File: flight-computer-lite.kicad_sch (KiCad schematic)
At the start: 18 parts, among them J1 USB_C_Receptacle_USB2.0_16P, J2 Micro_SD_Card_Det2, J3 Conn_01x02_Pin, Q1 BSS138, U1 RP2040, U2 W25Q32JVZP

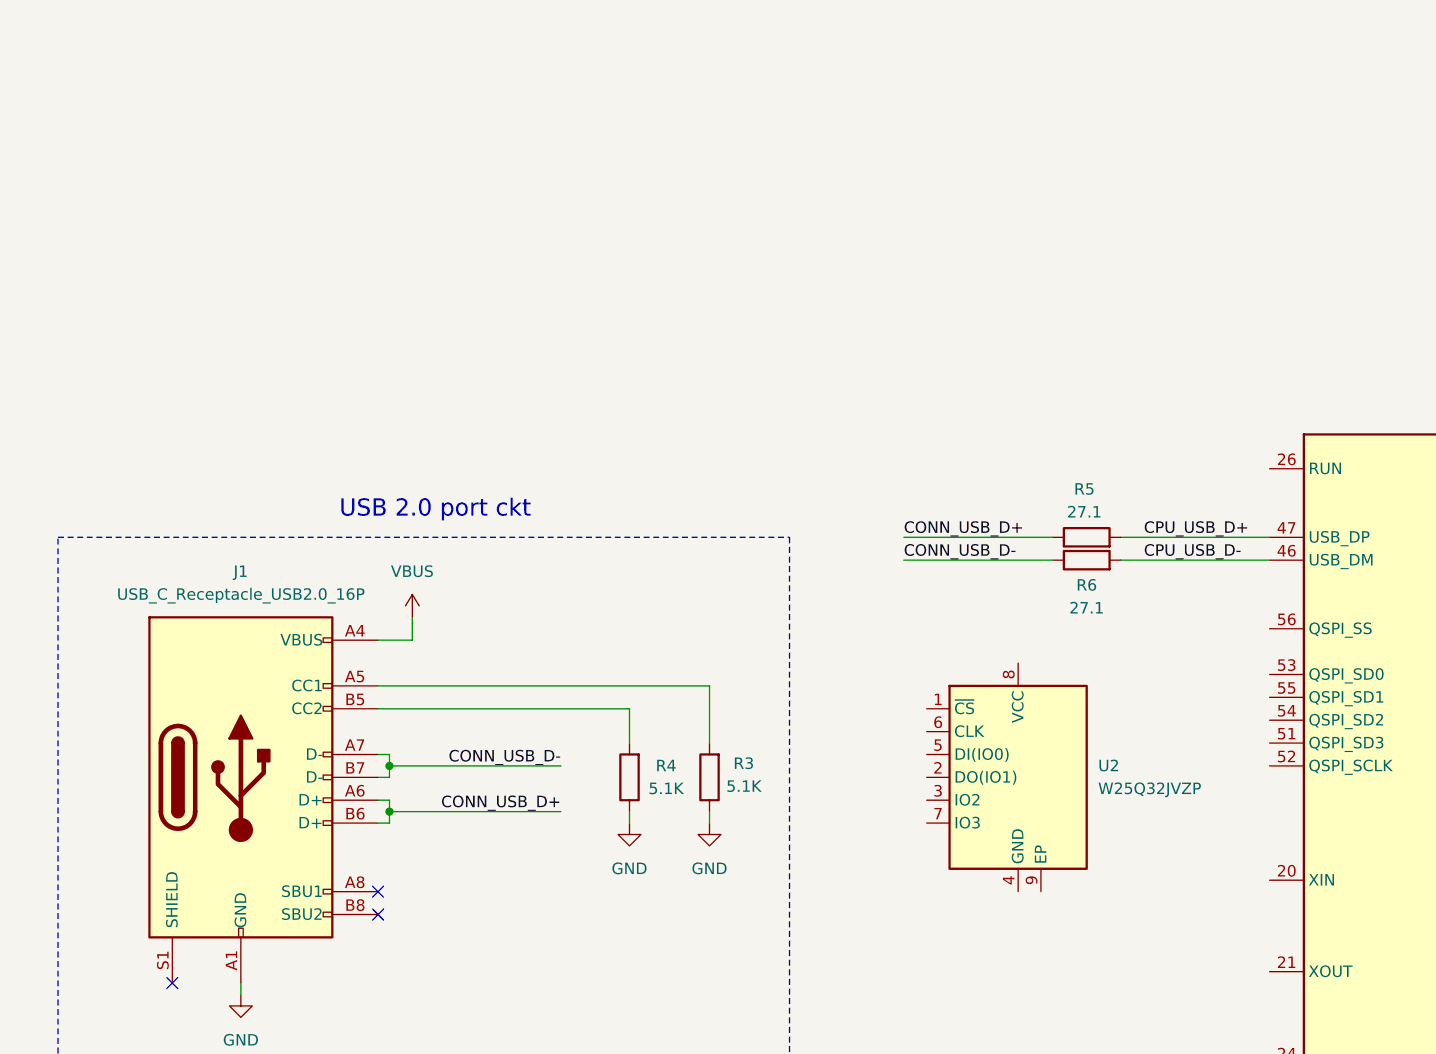
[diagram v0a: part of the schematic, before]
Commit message: Wired flash
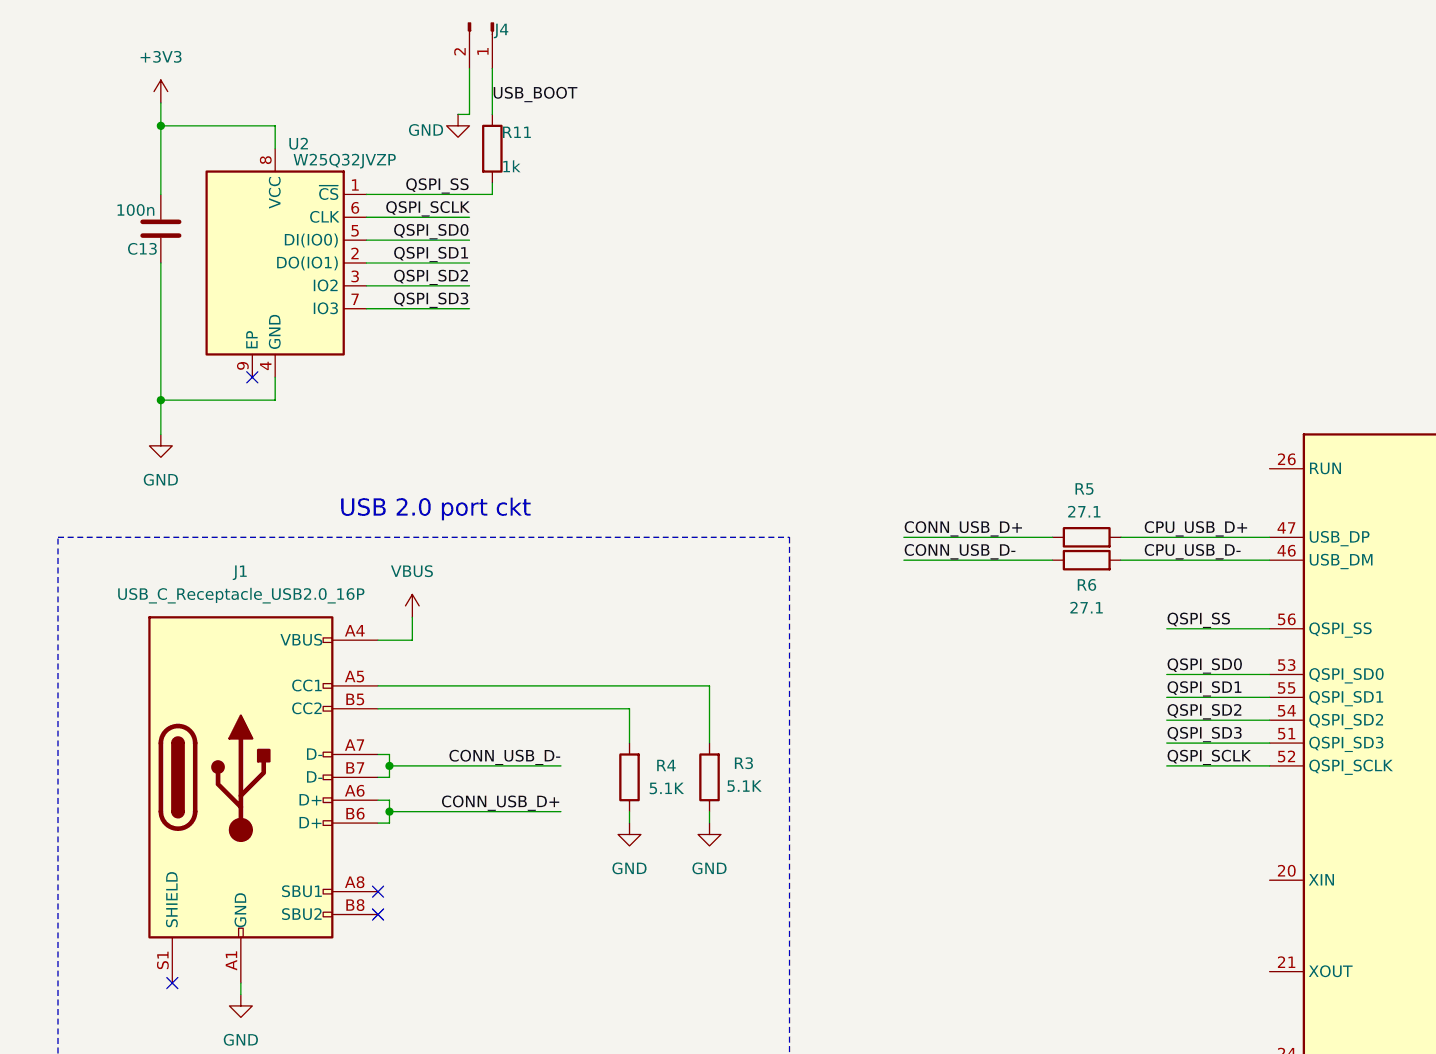
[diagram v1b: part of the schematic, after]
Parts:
- added C13: 100n, Capacitor_SMD:C_0603_1608Metric, symbol Device:C
- added J4: Conn_01x02_Pin, Connector_JST:JST_PH_S2B-PH-SM4-TB_1x02-1MP_P2.00mm_Horizontal, symbol Connector:Conn_01x02_Pin
- added R11: 1k, Resistor_SMD:R_0603_1608Metric, symbol Device:R
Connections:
- net +3V3: now also U2.8 (VCC), C13.1
- net GND: now also U2.4 (GND), C13.2, J4.2 (Pin_2)
- net QSPI_SS: now reaches U2.1 (~{CS})
- net QSPI_SS: now also U1.56 (QSPI_SS), R11.2
- net QSPI_SD1: now reaches U2.2 (DO(IO1))
- net QSPI_SD1: now also U1.55 (QSPI_SD1)
- net QSPI_SD2: now reaches U2.3 (IO2)
- net QSPI_SD2: now also U1.54 (QSPI_SD2)
- net QSPI_SD0: now reaches U2.5 (DI(IO0))
- net QSPI_SD0: now also U1.53 (QSPI_SD0)
- net QSPI_SCLK: now reaches U2.6 (CLK)
- net QSPI_SCLK: now also U1.52 (QSPI_SCLK)
- net QSPI_SD3: now reaches U2.7 (IO3)
- net QSPI_SD3: now also U1.51 (QSPI_SD3)
- new net USB_BOOT: J4.1 (Pin_1), R11.1
- no-connect marks 3 -> 4
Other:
- moved on the sheet: U2

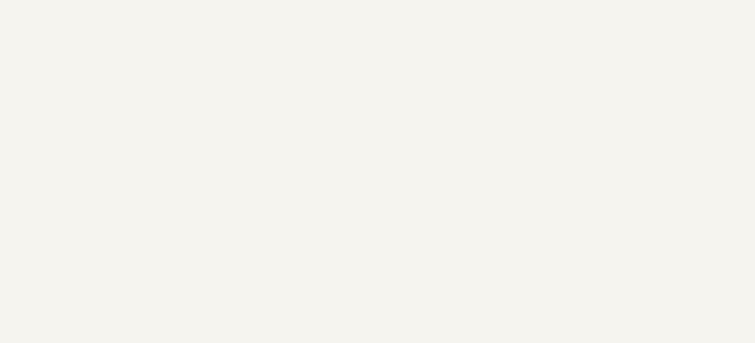
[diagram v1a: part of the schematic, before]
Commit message: Added buck-boost
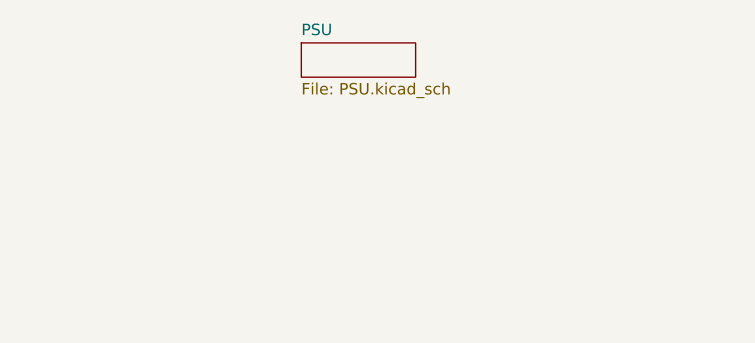
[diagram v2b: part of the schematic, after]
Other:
- added sheet PSU (PSU.kicad_sch)
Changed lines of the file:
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@@
 		)
 		(instances
-			(project ""
+			(project "flight-computer-lite"
 				(path "/68fb1519-f2e0-49f5-8b7c-4cc7366600ef"
 					(reference "#PWR030")
@@
 		)
 		(instances
-			(project ""
+			(project "flight-computer-lite"
 				(path "/68fb1519-f2e0-49f5-8b7c-4cc7366600ef"
 					(reference "J3")
@@
 		)
 		(instances
-			(project ""
+			(project "flight-computer-lite"
 				(path "/68fb1519-f2e0-49f5-8b7c-4cc7366600ef"
 					(reference "J4")
@@
 		)
 		(instances
-			(project ""
+			(project "flight-computer-lite"
 				(path "/68fb1519-f2e0-49f5-8b7c-4cc7366600ef"
 					(reference "U2")
@@
 		)
 		(instances
-			(project ""
+			(project "flight-computer-lite"
 				(path "/68fb1519-f2e0-49f5-8b7c-4cc7366600ef"
 					(reference "Q1")
@@
 		)
 		(instances
-			(project ""
+			(project "flight-computer-lite"
 				(path "/68fb1519-f2e0-49f5-8b7c-4cc7366600ef"
 					(reference "R4")
@@
 		)
 		(instances
-			(project ""
+			(project "flight-computer-lite"
 				(path "/68fb1519-f2e0-49f5-8b7c-4cc7366600ef"
 					(reference "BZ1")
@@
 		)
 		(instances
-			(project ""
+			(project "flight-computer-lite"
 				(path "/68fb1519-f2e0-49f5-8b7c-4cc7366600ef"
 					(reference "J1")
@@
 		)
 		(instances
-			(project ""
+			(project "flight-computer-lite"
 				(path "/68fb1519-f2e0-49f5-8b7c-4cc7366600ef"
 					(reference "#PWR05")
@@
 		)
 		(instances
-			(project ""
+			(project "flight-computer-lite"
 				(path "/68fb1519-f2e0-49f5-8b7c-4cc7366600ef"
 					(reference "D1")
@@
 		)
 		(instances
-			(project ""
+			(project "flight-computer-lite"
 				(path "/68fb1519-f2e0-49f5-8b7c-4cc7366600ef"
 					(reference "H1")
@@
 		)
 		(instances
-			(project ""
+			(project "flight-computer-lite"
 				(path "/68fb1519-f2e0-49f5-8b7c-4cc7366600ef"
 					(reference "R11")
@@
 		)
 		(instances
-			(project ""
+			(project "flight-computer-lite"
 				(path "/68fb1519-f2e0-49f5-8b7c-4cc7366600ef"
 					(reference "U1")
@@
 		)
 		(instances
-			(project ""
+			(project "flight-computer-lite"
 				(path "/68fb1519-f2e0-49f5-8b7c-4cc7366600ef"
 					(reference "J2")
@@
 		)
 		(instances
-			(project ""
+			(project "flight-computer-lite"
 				(path "/68fb1519-f2e0-49f5-8b7c-4cc7366600ef"
 					(reference "#PWR019")
@@
 		)
 		(instances
-			(project ""
+			(project "flight-computer-lite"
 				(path "/68fb1519-f2e0-49f5-8b7c-4cc7366600ef"
 					(reference "#PWR04")
@@
 		)
 		(instances
-			(project ""
+			(project "flight-computer-lite"
 				(path "/68fb1519-f2e0-49f5-8b7c-4cc7366600ef"
 					(reference "#PWR029")
@@
 		)
 		(instances
-			(project ""
+			(project "flight-computer-lite"
 				(path "/68fb1519-f2e0-49f5-8b7c-4cc7366600ef"
 					(reference "#PWR028")
@@
 		)
 		(instances
-			(project ""
+			(project "flight-computer-lite"
 				(path "/68fb1519-f2e0-49f5-8b7c-4cc7366600ef"
 					(reference "R3")
@@
 		)
 		(instances
-			(project ""
+			(project "flight-computer-lite"
 				(path "/68fb1519-f2e0-49f5-8b7c-4cc7366600ef"
 					(reference "R1")
@@
 		)
 		(instances
-			(project ""
+			(project "flight-computer-lite"
 				(path "/68fb1519-f2e0-49f5-8b7c-4cc7366600ef"
 					(reference "#PWR020")
@@
 				)
 			)
+		)
+	)
+	(sheet
+		(at 228.6 21.59)
+		(size 12.7 3.81)
+		(fields_autoplaced yes)
+		(stroke
+			(width 0.1524)
+			(type solid)
+		)
+		(fill
+			(color 0 0 0 0.0000)
+		)
+		(property "Sheetname" "PSU"
+			(at 228.6 20.8784 0)
+			(effects
+				(font
+					(size 1.27 1.27)
+				)
+				(justify left bottom)
+			)
+		)
+		(property "Sheetfile" "PSU.kicad_sch"
+			(at 228.6 25.9846 0)
+			(effects
+				(font
+					(size 1.27 1.27)
+				)
+				(justify left top)
+			)
+		)
+		(instances
+			(project "flight-computer-lite"
+				(path "/68fb1519-f2e0-49f5-8b7c-4cc7366600ef"
+					(page "4")
+				)
+			)

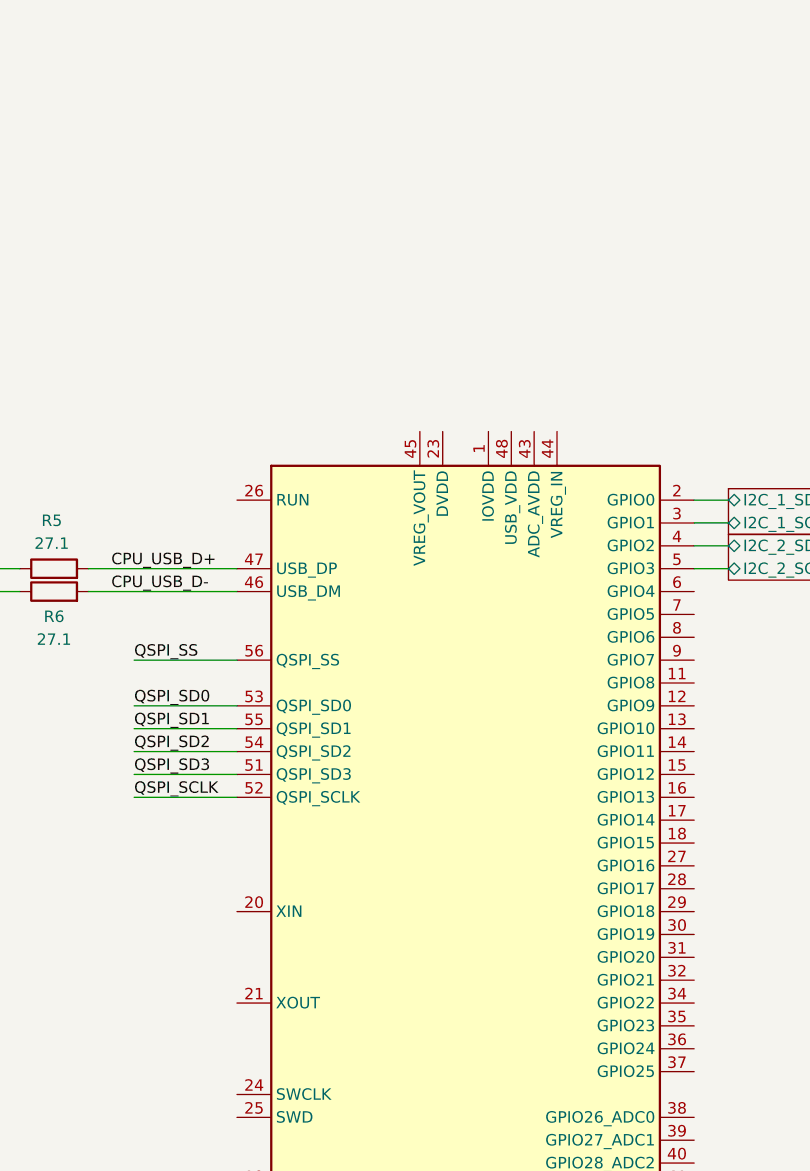
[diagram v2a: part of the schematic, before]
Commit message: Finished PSU
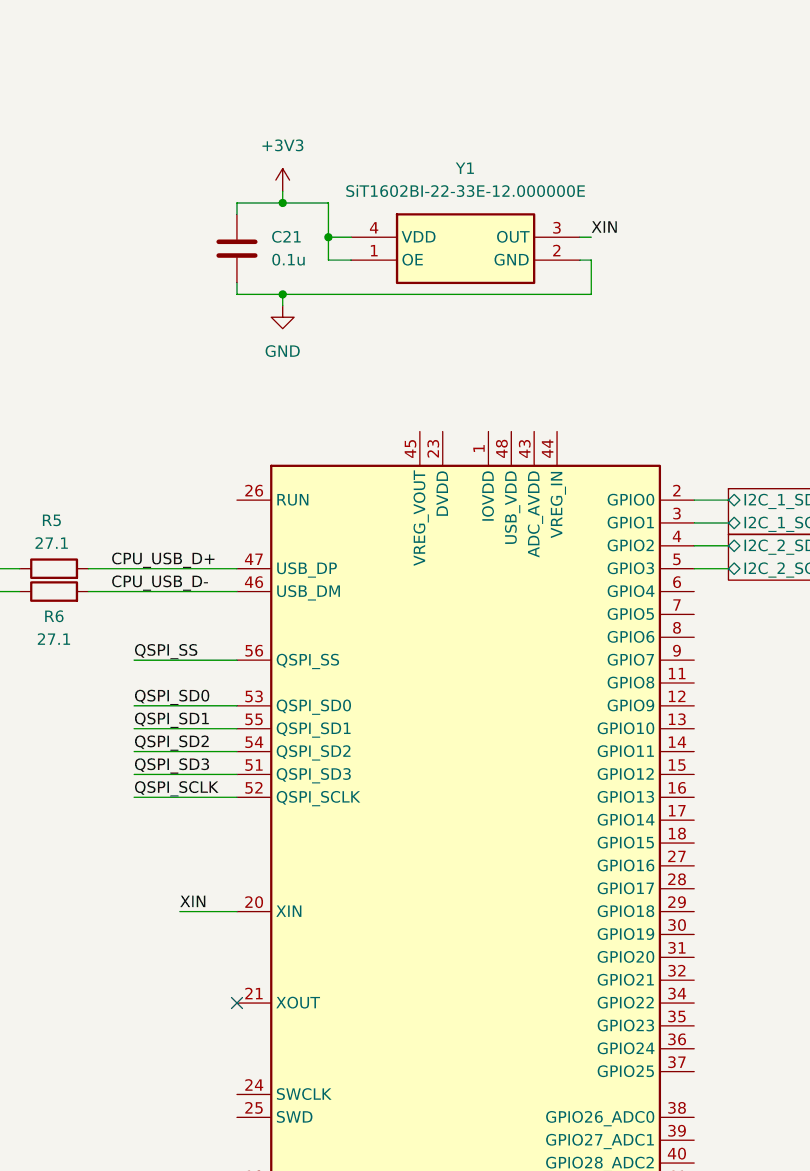
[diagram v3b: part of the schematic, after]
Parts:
- added C21: 0.1u, Capacitor_SMD:C_0603_1608Metric, symbol Device:C
- added Y1: SiT1602BI-22-33E-12.000000E, LRI_partlib:SIT1602BI2233E12000000G, symbol SiT1602BI:SiT1602BI-22-33E-12.000000E
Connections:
- net +3V3: now also C21.1, Y1.1 (OE), Y1.4 (VDD)
- net GND: now also C21.2, Y1.2 (GND)
- net XIN: now reaches U1.20 (XIN)
- net XIN: now also Y1.3 (OUT)
- no-connect marks 4 -> 5
